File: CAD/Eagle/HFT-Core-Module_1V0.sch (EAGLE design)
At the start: 267 parts, among them Q0521 ABS07-32.768KHZ, Q0911 ABM3B-16MHZ-10-R50-1-U, U0111 STM32L4Z_144PIN_SMPS, U0431 PAM2305AAB120, U0601 LM4120IM5-3.0, U0611 MAX5217, U0631 CFPT-141-20MHZ, U0641 OPA354, U0901 AX5243, U1001 AX5243, U1601 SPV1040T, U1701 TS5A23166, U1801 PAM2305AAB330, U1901 TS5A23166, U2001 TS5A23166, U2101 TS5A23166, X511 2X20/90_1MM27_HARWIN_M50-3202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, X512 2X20/90_1MM27_HARWIN_M50-3202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, X521 2X20/90_1MM27_HARWIN_M50-3202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, X522 2X20/90_1MM27_HARWIN_M50-3202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, X531 2X20/90_1MM27_HARWIN_M50-3202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, X532 2X20/90_1MM27_HARWIN_M50-3202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

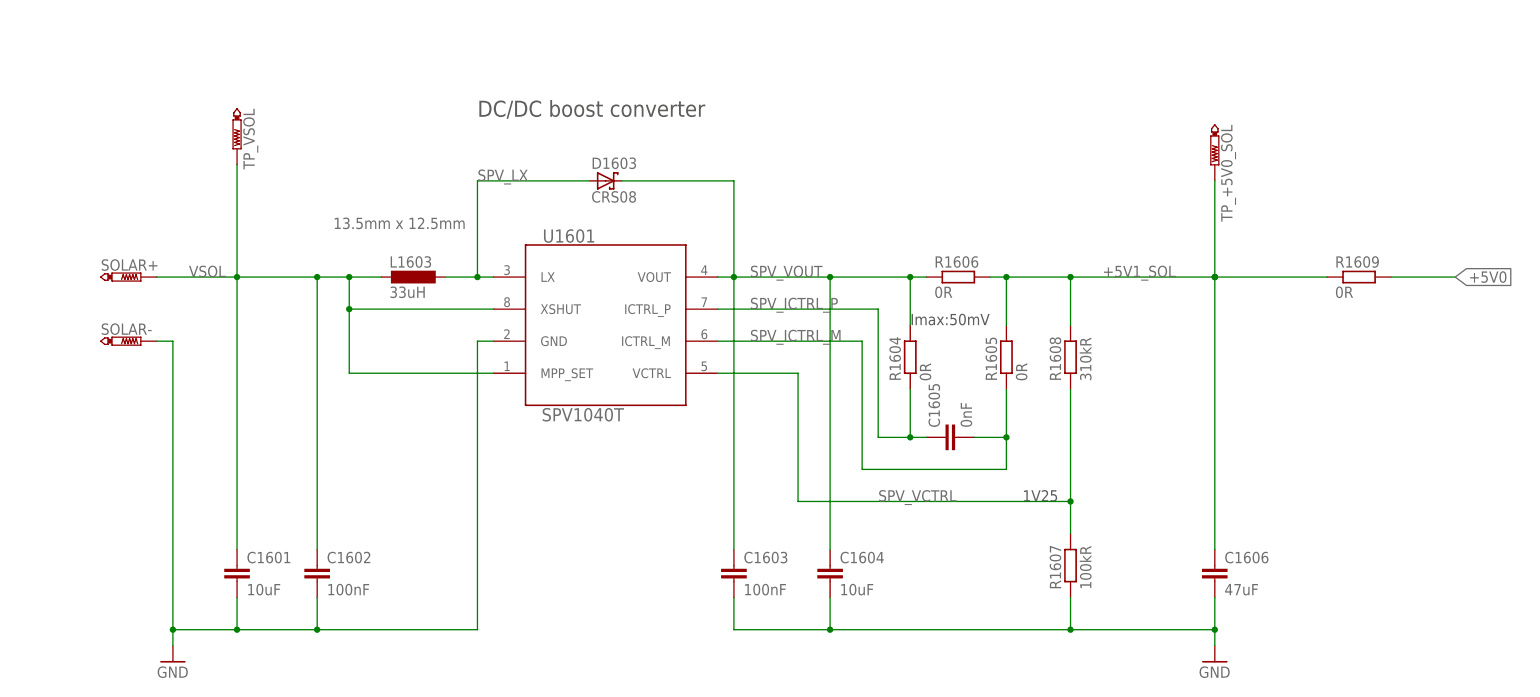
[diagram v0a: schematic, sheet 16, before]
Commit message: HW_1V0 - first placement for solar panel and dc/dc boost converter
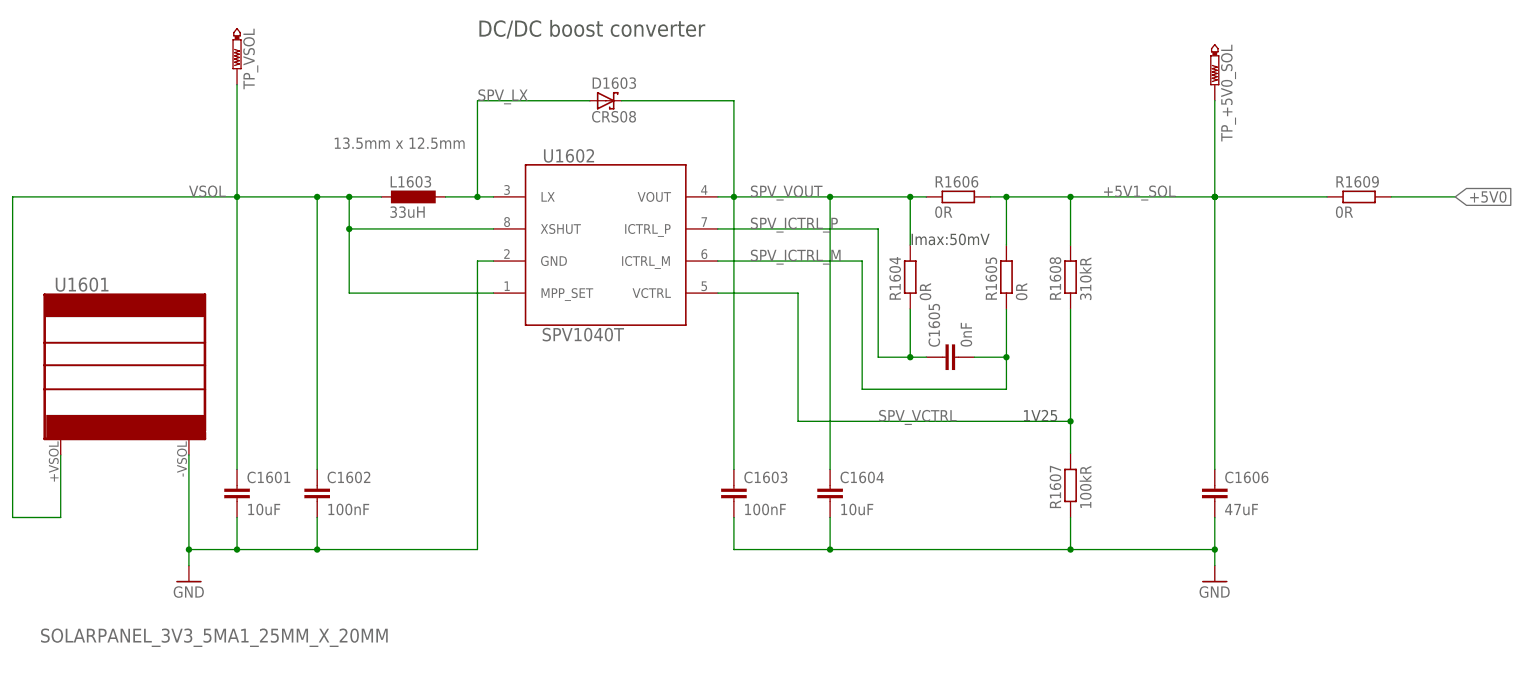
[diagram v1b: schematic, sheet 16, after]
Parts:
- removed SOLAR+, SOLAR-: PTR1PAD1-20, testpad:PTR1PAD1-20
- added TP_+3V3: PTR1B1,27, testpad:PTR1B1,27
- added U0801: NHD-C0220BIZ_2X20CHARS, df4iah_lcd:NHD-C0220BIZ_2X20CHARS
- added U1602: SPV1040T, df4iah_powersupply:SPV1040
- TP_+5V0, TP_+5V0_SOL, TP_+5V0_USB_SW, TP_VSOL: value PTR1TP06R -> PTR1B1,27; device testpad:PTR1TP06R -> testpad:PTR1B1,27
- U1601: value SPV1040T -> SOLARPANEL_3V3_5MA1_25MM_X_20MM; device df4iah_powersupply:SPV1040 -> df4iah_supply:SOLARPANEL_3V3_5MA1_25MM_X_20MM
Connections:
- net +3V3: now also TP_+3V3.TP, U0801.VDD
- net GND: now also U0801.VSS, U1601.-VSOL, U1602.GND; no longer SOLAR-.TP, U1601.GND
- net LCD_!RST: now also U0801.RST
- net MCU_I2C1_SCL: now also U0801.SCL
- net MCU_I2C1_SDA: now also U0801.SDA
- net N$6: now also U0801.C1-
- net N$7: now also U0801.C1+
- net N$8: now also U0801.VOUT
- net SPV_ICTRL_M: now also U1602.ICTRL_M; no longer U1601.ICTRL_M
- net SPV_ICTRL_P: now also U1602.ICTRL_P; no longer U1601.ICTRL_P
- net SPV_LX: now also U1602.LX; no longer U1601.LX
- net SPV_VCTRL: now also U1602.VCTRL; no longer U1601.VCTRL
- net SPV_VOUT: now also U1602.VOUT; no longer U1601.VOUT
- net VSOL: now also U1601.+VSOL, U1602.MPP_SET, U1602.XSHUT; no longer SOLAR+.TP, U1601.MPP_SET, U1601.XSHUT
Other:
- note added: "LCD: 2x20 chars NHD-C0220BIZ-FS(RGB)-FBW-3VM-ND"
- note removed: "1"
- note removed: "2"
- note removed: "3"
- note removed: "4"
- note removed: "5"
- note removed: "6"
- note removed: "7"
- note removed: "8"
- note removed: "Use LCD 20x2 NHD-C0220BIZ-FS(RGB)-FBW-3VM-ND"
- moved on the sheet: C0811, C0821, C0831, C1601, C1602, C1603, C1604, C1605, C1606, D1603, L1603, R1604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

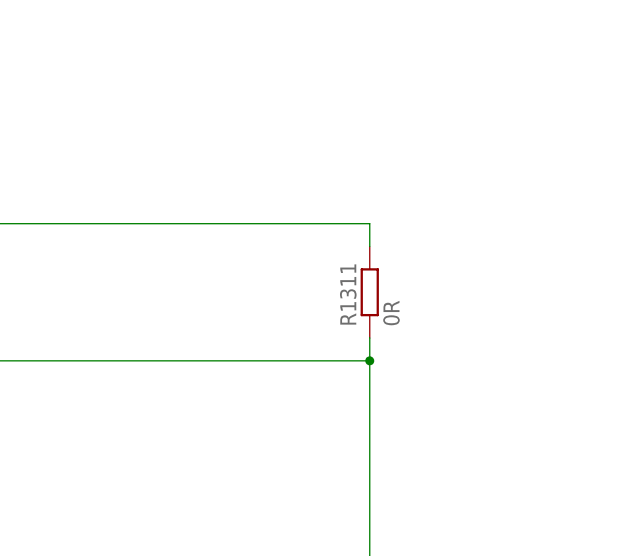
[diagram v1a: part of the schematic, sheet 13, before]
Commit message: HW_1V0 - some placements done
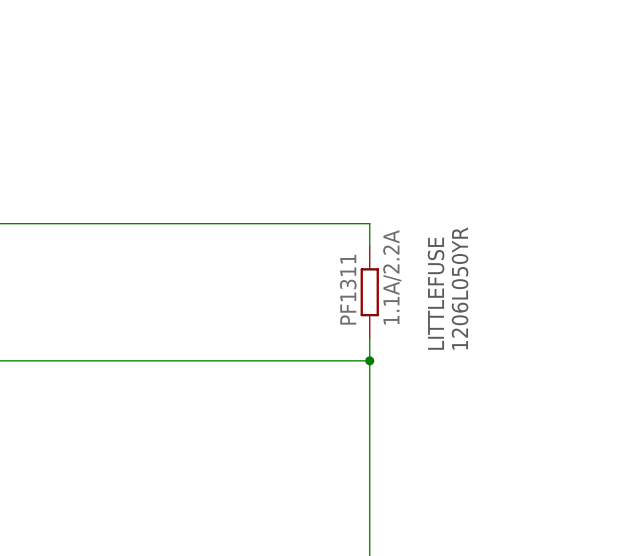
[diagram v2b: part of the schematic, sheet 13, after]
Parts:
- removed R1311: 0R, df4iah_rcl:R-EU_R0603
- added PF1311: 1.1A/2.2A, rcl:R-EU_M1206
- R1302: device df4iah_rcl:R-EU_R0603 -> rcl:R-EU_R0603
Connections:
- net MCU_VDDUSB: now also PF1311.1; no longer R1311.1
- net PA9: now also PF1311.2; no longer R1311.2
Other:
- note added: "LITTLEFUSE 1206L050YR"
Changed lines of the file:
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@@
 <part name="U1801" library="df4iah_powersupply" deviceset="PAM2305" device="" value="PAM2305AAB330"/>
 <part name="U1602" library="df4iah_powersupply" deviceset="SPV1040" device="" value="SPV1040T"/>
-<part name="R1302" library="df4iah_rcl" deviceset="R-EU_" device="R0603" value="330kR"/>
+<part name="R1302" library="rcl" deviceset="R-EU_" device="R0603" value="330kR"/>
 <part name="C1303" library="df4iah_rcl" deviceset="C-EU" device="C0603" value="1nF"/>
 <part name="FRAME9" library="df4iah_frame" deviceset="A4L-LOC" device="" value="Holes"/>
@@
 <part name="GND0002" library="df4iah_supply" deviceset="GND" device=""/>
 <part name="R0251" library="rcl" deviceset="R-EU_" device="R0603" value="47R"/>
-<part name="R1311" library="df4iah_rcl" deviceset="R-EU_" device="R0603" value="0R"/>
 <part name="U0611" library="df4iah_dac" deviceset="MAX5217" device=""/>
 <part name="TP_+3V3" library="testpad" deviceset="PTR1" device="B1,27" value="PTR1B1,27"/>
 <part name="U1601" library="df4iah_supply" deviceset="SOLARPANEL_3V3_5MA1_25MM_X_20MM" device=""/>
 <part name="U0801" library="df4iah_lcd" deviceset="NHD-C0220BIZ_2X20CHARS" device=""/>
+<part name="PF1311" library="rcl" deviceset="R-EU_" device="M1206" value="1.1A/2.2A"/>
 </parts>
 <sheets>
@@
 <text x="48.26" y="132.08" size="1.778" layer="97">MCU_VDDUSB</text>
 <text x="48.26" y="147.32" size="1.778" layer="97">MCU_USB_OTG_FS_VBUS</text>
+<text x="186.182" y="133.096" size="1.778" layer="97" rot="R90">LITTLEFUSE
+1206L050YR</text>
 </plain>
 <instances>
@@
 <instance part="R1302" gate="G$1" x="185.42" y="71.12"/>
 <instance part="C1303" gate="G$1" x="185.42" y="58.42" rot="R90"/>
-<instance part="R1311" gate="G$1" x="175.26" y="139.7" rot="R90"/>
+<instance part="PF1311" gate="G$1" x="175.26" y="139.7" rot="R90"/>
 </instances>
 <busses>
@@
 <label x="43.18" y="132.08" size="1.778" layer="95" rot="R180" xref="yes"/>
 <wire x1="175.26" y1="132.08" x2="175.26" y2="134.62" width="0.1524" layer="91"/>
-<pinref part="R1311" gate="G$1" pin="1"/>
 <junction x="175.26" y="132.08"/>
+<pinref part="PF1311" gate="G$1" pin="1"/>
 </segment>
 </net>
@@
 <net name="PA9" class="0">
 <segment>
-<pinref part="R1311" gate="G$1" pin="2"/>
 <wire x1="175.26" y1="144.78" x2="175.26" y2="147.32" width="0.1524" layer="91"/>
 <wire x1="175.26" y1="147.32" x2="43.18" y2="147.32" width="0.1524" layer="91"/>
 <label x="43.18" y="147.32" size="1.778" layer="95" rot="R180" xref="yes"/>
+<pinref part="PF1311" gate="G$1" pin="2"/>
 </segment>
 </net>

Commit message: HW_1V0 - work of the day
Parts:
- removed R0745: 0R, rcl:R-EU_R0603
- added C1111, C1112, C1701: 100nF, rcl:C-EUC0603
- added C1113: 47pF, rcl:C-EUC0603
- added L1112: 10uH, rcl:L-EUL2012C
- added R1114: 47R, rcl:R-EU_R0603
- added R1131, R1132, R1136, R1137: 10kR, rcl:R-EU_R0603
- added TP_+1V2, TP_+1V2_MCU, TP_+3V3_20MHZ, TP_+3V3_HICUR, TP_VBAT: PTR1B1,27, testpad:PTR1B1,27
- added U0701: SI5338, df4iah_osc:SI5338
- added U1111: MAX5136AGTG+, df4iah_dac:MAX5136
- added U1130, U1131, U1136: OPA354, df4iah_opamp:OPA354
- added X1501, X1511: CUI SJ1-3535NS, df4iah_connector:SJ1-353XNS_3MM5-STEREO-AUDIO-JACKS
- C0313: value 1nF -> 100nF
- R0311: value 10kR -> 3.3kR
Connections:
- net N$6 renamed LCD_C1-
- net N$7 renamed LCD_C1+
- net N$8 renamed LCD_VOUT
- removed net MCU_VDDUSB: PF1311.1, U0111.VDDUSB, U1701.1, U1701.5, U1701.8, X1301.J_VUSB
- removed net SI5338_RSVD_GND: R0745.1
- new net AUDIO_IN_L: X1501.TIP
- new net AUDIO_IN_R: X1501.RING
- new net AUDIO_OUT_L: R1132.2, U1131.OUT, X1511.TIP
- new net AUDIO_OUT_R: R1137.2, U1136.OUT, X1511.RING
- new net MAX5136_!READY: R1114.2, U1111.!READY
- new net MAX5136_AVDD: C1112.2, L1112.1, U1111.AVDD, U1111.M/!Z
- new net MAX5136_OUT0: U1111.OUT0, U1131.+IN
- new net MAX5136_OUT1: U1111.OUT1, U1136.+IN
- new net MAX5136_OUT_L_FB: R1131.2, R1132.1, U1131.-IN
- new net MAX5136_OUT_R_FB: R1136.2, R1137.1, U1136.-IN
- new net MAX5136_REF: C1113.1, U1111.REFI, U1111.REFO, U1130.+IN
- new net MAX5136_REF_OP: R1131.1, R1136.1, U1130.-IN, U1130.OUT
- new net MCU_SPI1_AUDIO_DAC_!RDY: R1114.1
- new net MCU_SPI1_AUDIO_DAC_SEL: U1111.!CS
- new net VDDUSB: PF1311.2, U0111.VDDUSB, U1701.1, U1701.5, U1701.8
- net +1V2: now also TP_+1V2.TP
- net +3V3_20MHZ: now also TP_+3V3_20MHZ.TP
- net +3V3_HICUR: now also C1111.1, L1112.2, TP_+3V3_HICUR.TP, U0701.VDD@24, U0701.VDD@7, U0701.VDDO0, U0701.VDDO1, U0701.VDDO2, U0701.VDDO3, U1111.!LDAC, U1111.DVDD, U1130.V+, U1131.V+, U1136.V+
- net GND: now also C1111.2, C1112.1, C1113.2, C1701.2, U0701.PAD, U0701.RSVD_GND, U1111.GND, U1130.V-, U1131.V-, U1136.V-, X1501.GND, X1501.SLEEVE, X1511.GND, X1511.SLEEVE; no longer R0745.2
- net MCU_I2C1_SCL: now also U0701.SCL
- net MCU_I2C1_SDA: now also U0701.SDA
- net MCU_INTR_SI5338: now also U0701.INTR
- net MCU_SPI1_CLK: now also U1111.SCLK
- net MCU_SPI1_MOSI: now also U1111.DIN
- net MCU_VBAT: now also TP_VBAT.TP
- net MCU_VDD12: now also TP_+1V2_MCU.TP
- net MCU_VUSB_EN: now also C1701.1
- net PA9: now also PF1311.1, X1301.J_VUSB; no longer PF1311.2
- net SI5338_CLK0A: now also U0701.CLK0A
- net SI5338_CLK0B: now also U0701.CLK0B
- net SI5338_CLK1A: now also U0701.CLK1A
- net SI5338_CLK1B: now also U0701.CLK1B
- net SI5338_CLK2A: now also U0701.CLK2A
- net SI5338_CLK2B: now also U0701.CLK2B
- net SI5338_CLK3A: now also U0701.CLK3A
- net SI5338_CLK3B: now also U0701.CLK3B
- net SI5338_IN1: now also U0701.IN1
- net SI5338_IN2: now also U0701.IN2
- net SI5338_IN3: now also U0701.IN3
- net SI5338_IN4: now also U0701.IN4
- net SI5338_IN5: now also U0701.IN5
- net SI5338_IN6: now also U0701.IN6
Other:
- note added: "AUDIO IN"
- note added: "AUDIO OUT"
- note removed: "INPUT"
- note removed: "MCU_VDDUSB"
- note removed: "OUTPUT"
- note removed: "Use CUI SJ1-3535NS"
- note removed: "Use PLL Si5338"

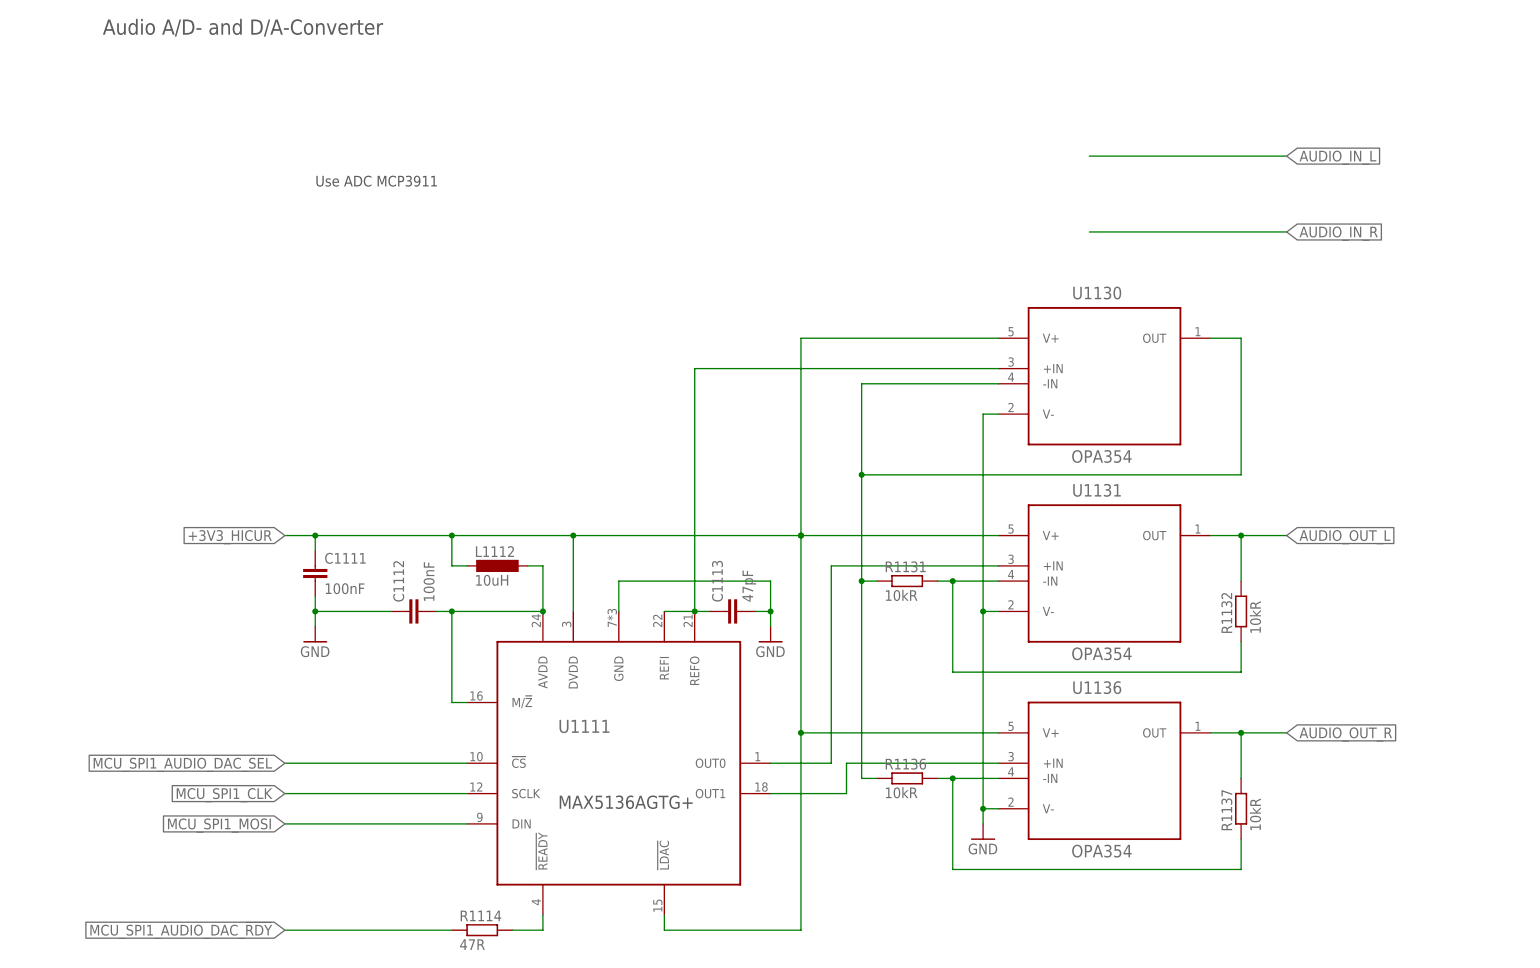
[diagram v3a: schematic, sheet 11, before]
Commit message: HW_1V0 - Audio DAC added
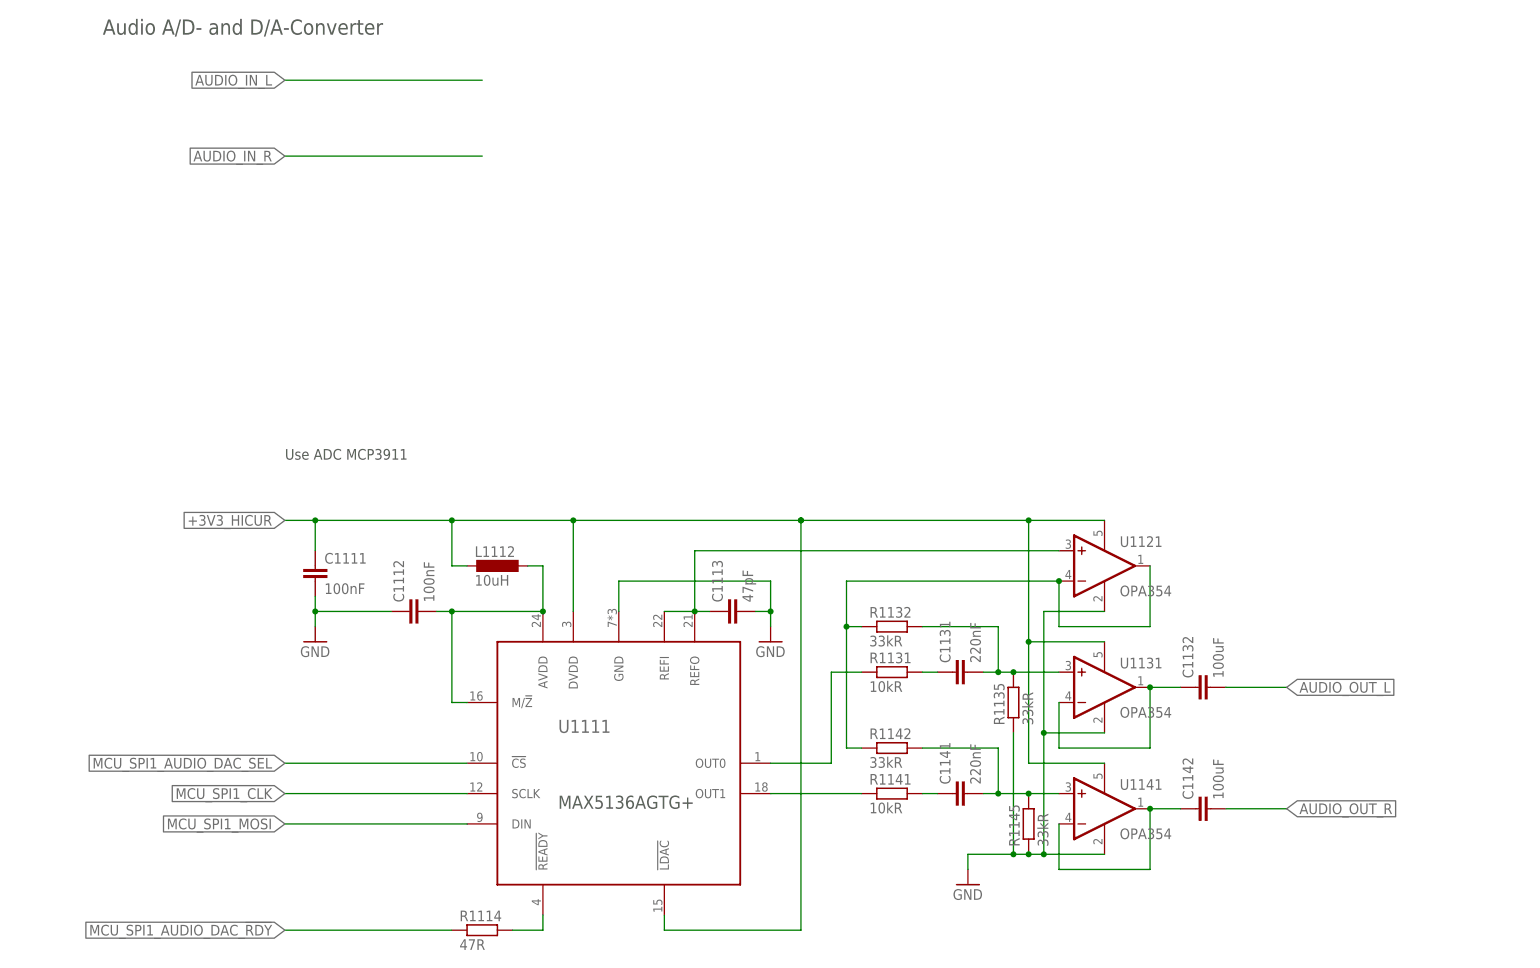
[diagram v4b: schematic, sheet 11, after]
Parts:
- removed R1136, R1137: 10kR, rcl:R-EU_R0603
- removed U1130, U1136: OPA354, df4iah_opamp:OPA354
- added C1131, C1141: 220nF, df4iah_rcl:C-EUC0603
- added C1132, C1142: 100uF, df4iah_rcl:C-EUC0805
- added R1135, R1142, R1145: 33kR, rcl:R-EU_R0603
- added R1141: 10kR, rcl:R-EU_R0603
- added U1121, U1141: OPA354, df4iah_opamp:OPA354
- R1132: value 10kR -> 33kR
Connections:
- removed net MAX5136_OUT_L_FB: R1131.2, R1132.1, U1131.-IN
- removed net MAX5136_OUT_R_FB: R1136.2, R1137.1, U1136.-IN
- new net AUDIO_OUT_L_OP: C1132.1, U1131.-IN, U1131.OUT
- new net AUDIO_OUT_R_OP: C1142.1, U1141.-IN, U1141.OUT
- new net MAX5136_OUT0_R: C1131.1, R1131.2
- new net MAX5136_OUT0_SUM: C1131.2, R1132.2, R1135.2, U1131.+IN
- new net MAX5136_OUT1_R: C1141.1, R1141.2
- new net MAX5136_OUT1_SUM: C1141.2, R1142.2, R1145.2, U1141.+IN
- net +3V3_HICUR: now also U1121.V+, U1141.V+; no longer U1130.V+, U1136.V+
- net AUDIO_OUT_L: now also C1132.2; no longer R1132.2, U1131.OUT
- net AUDIO_OUT_R: now also C1142.2; no longer R1137.2, U1136.OUT
- net GND: now also R1135.1, R1145.1, U1121.V-, U1141.V-; no longer U1130.V-, U1136.V-
- net MAX5136_OUT0: now also R1131.1; no longer U1131.+IN
- net MAX5136_OUT1: now also R1141.1; no longer U1136.+IN
- net MAX5136_REF: now also U1121.+IN; no longer U1130.+IN
- net MAX5136_REF_OP: now also R1132.1, R1142.1, U1121.-IN, U1121.OUT; no longer R1131.1, R1136.1, U1130.-IN, U1130.OUT
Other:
- moved on the sheet: R1131, R1132
